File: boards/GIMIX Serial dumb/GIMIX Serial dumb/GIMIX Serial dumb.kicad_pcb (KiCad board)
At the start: 2 copper layers, 132.4 x 88.4 mm, 48 parts, among them J1 RS232 Port, J2 Conn_01x13, J3 RS232 Port, J4 Conn_01x13, J5 Power, P1 SS30 Bus, U1 LM7805_TO220, U10 L7912, U2 75189, U3 MC6850_new, U4 MC6850_new, U5 75188, U6 75189, U7 74LS02, U8 74LS02, U9 L7812

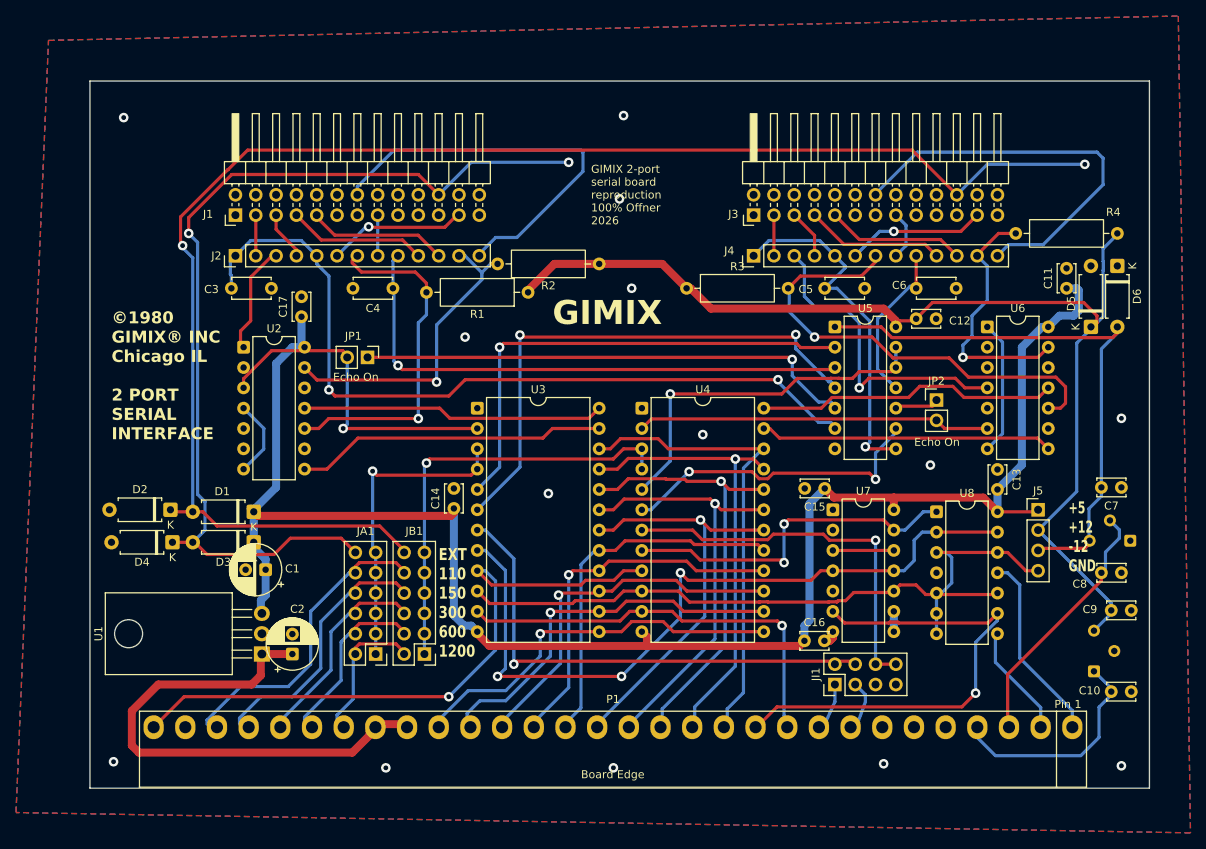
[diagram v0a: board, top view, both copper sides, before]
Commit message: dumb serial board small silkscreen changes
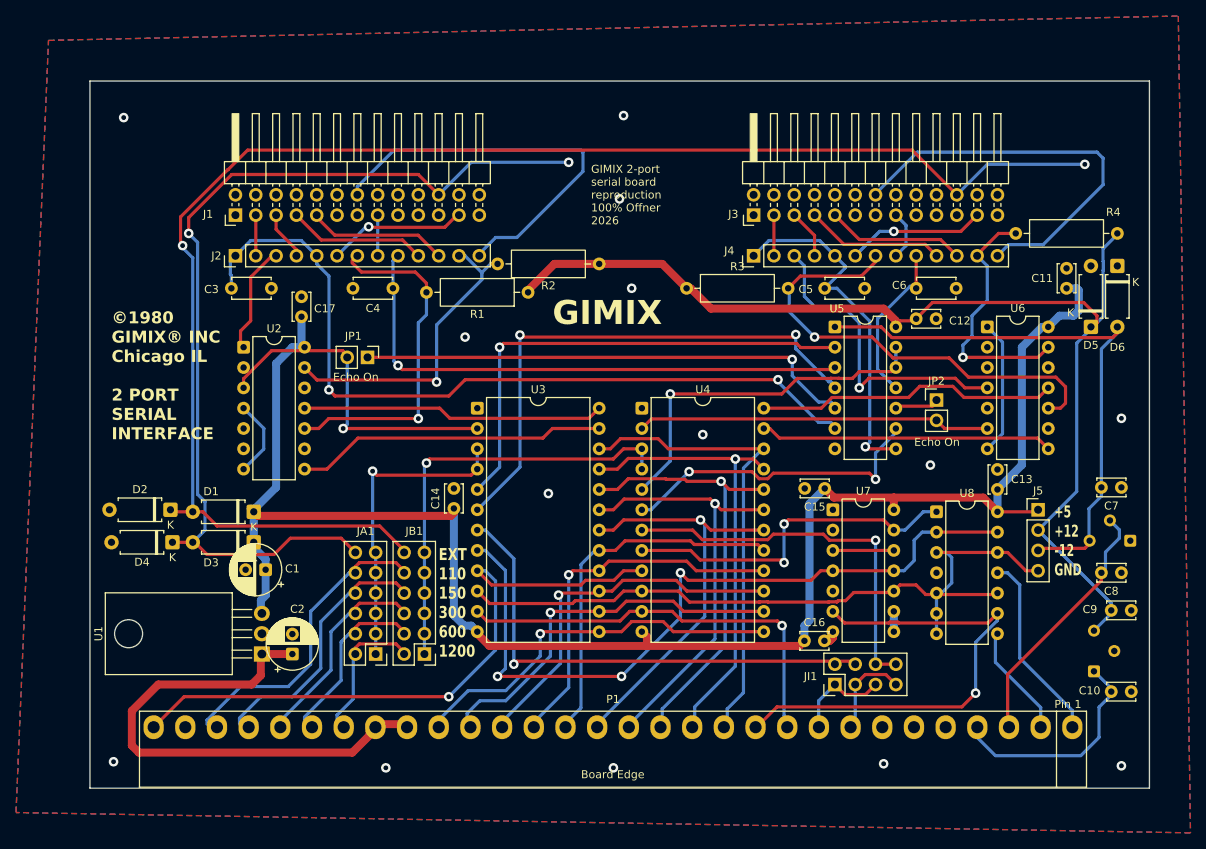
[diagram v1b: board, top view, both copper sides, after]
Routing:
- net /~{IRQ}: track 5.23 -> 12.3 mm
- net /~{FIRQ}: track 5.66 -> 11.7 mm
